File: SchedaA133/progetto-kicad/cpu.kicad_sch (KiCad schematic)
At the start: 77 parts, among them J301 UART0 debug, SW301 RESET, SW302 FEL, U301 A133, U302 TPD4E05U06DQA, U303 TPD4E05U06DQA, U304 TPD4E05U06DQA, U305 TPD4E05U06DQA, U306 TPD4E05U06DQA, U307 TPD4E05U06DQA, Y301 24MHz, Y302 32.768kHz

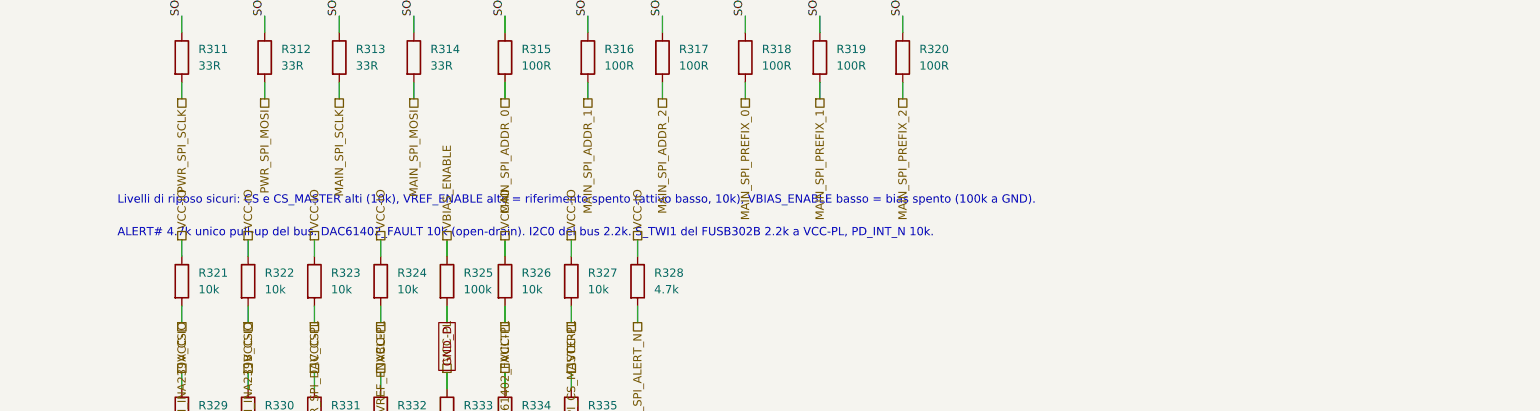
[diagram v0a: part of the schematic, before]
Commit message: SchedaA133: VREF_ENABLE attivo alto e FPC XUNPU
R324 da pull-up a pull-down 10k (VREF_ENABLE ora attivo alto sul modulo
Power). J2 MAIN con footprint XUNPU FPC-05F-28PH20 (LCSC C2856807) al
posto dell'Hirose provvisorio. Schema PDF rigenerato, ERC 0.

Co-Authored-By: Claude Opus 5.5 (1M context) <noreply@anthropic.com>
Claude-Session: https://claude.ai/code/session_01J3krgWFTUEjwvCnwUp9cQn
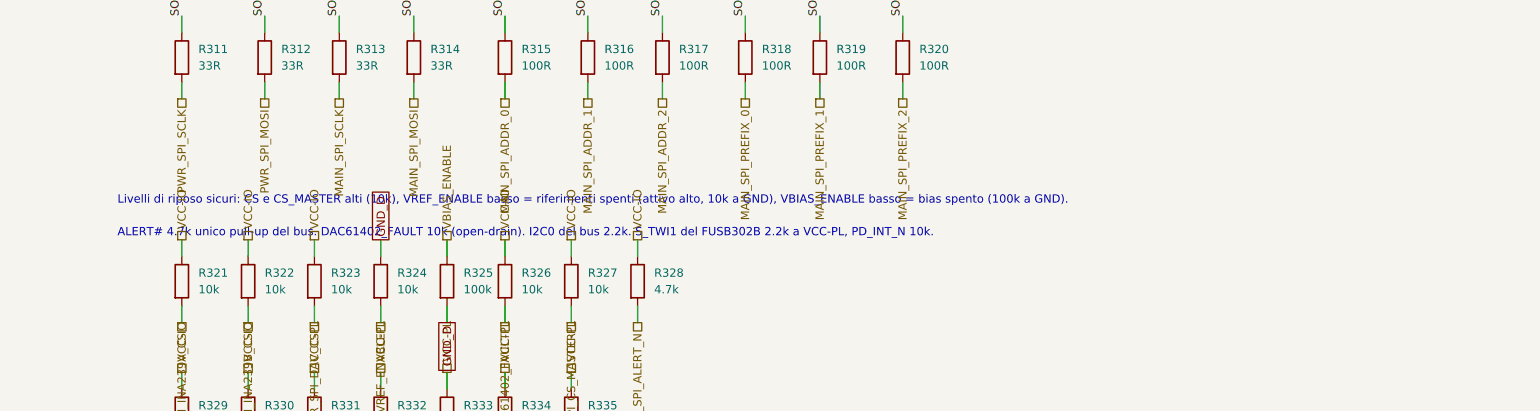
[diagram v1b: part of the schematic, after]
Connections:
- net GND_D: now also R324.1
- net VCC-IO: no longer R324.1
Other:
- note added: "Livelli di riposo sicuri: CS e CS_MASTER alti (10k), VREF_ENABLE basso = riferimenti spenti (attivo alto, 10k a GND), VBIAS_ENABLE basso = bias spento (100k a GND)."
- note removed: "Livelli di riposo sicuri: CS e CS_MASTER alti (10k), VREF_ENABLE alto = riferimento spento (attivo basso, 10k), VBIAS_ENABLE basso = bias spento (100k a GND)."

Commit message: Bus MIKILAB REV5.1: linea di coincidenza HIT# sul pin 28 del MAIN
Specifica: pin 28 (prima GND ridondante) = HIT#, open-drain attivo basso,
pull-up unico 4.7k sul master, impulso 100-200 ns per evento; logica di
coincidenza documentata (fronte marcato dal master, lettura dei latch).
PianoTest: HIT -> monostabile 74LVC1G123 (2k + 27 pF) -> 74LVC1G06 su
HIT#, passante J_IN -> J_OUT, ESD. ERC 0.
SchedaA133: J2 pin 28 -> PD4 (PD_EINT4), pull-up R336 4.7k, ESD su U307,
R337 0R DNP verso l'EXTINT del NEO-F10T. ERC 0, PDF rigenerato.
Documentazione bus della A133 e articolo (sezione bus e coincidenze)
aggiornati; corretta l'identita del primo piano (0).

Co-Authored-By: Claude Opus 5.5 (1M context) <noreply@anthropic.com>
Claude-Session: https://claude.ai/code/session_01J3krgWFTUEjwvCnwUp9cQn
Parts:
- added R336: 4.7k, Resistor_SMD:R_0402_1005Metric, symbol Device:R
- added R337: 0R, Resistor_SMD:R_0402_1005Metric, symbol Device:R
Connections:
- net VCC-IO: now also R336.1
- net MAIN_HIT_N: now reaches U307.4 (D2+)
- net MAIN_HIT_N: now also U301.AA22 (PD4), R336.2, R337.1
- new net GNSS_STROBE_R: R337.2
- no-connect marks 104 -> 102
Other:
- note added: "HIT# (MAIN pin 28, REV5.1): open-drain attivo basso, pull-up unico 4.7k (R336), su PD4 (PD_EINT4). R337 DNP: HIT# anche sull'ingresso time mark del NEO-F10T (EXTINT, fronte di discesa); montarlo solo senza STROBE esterno."

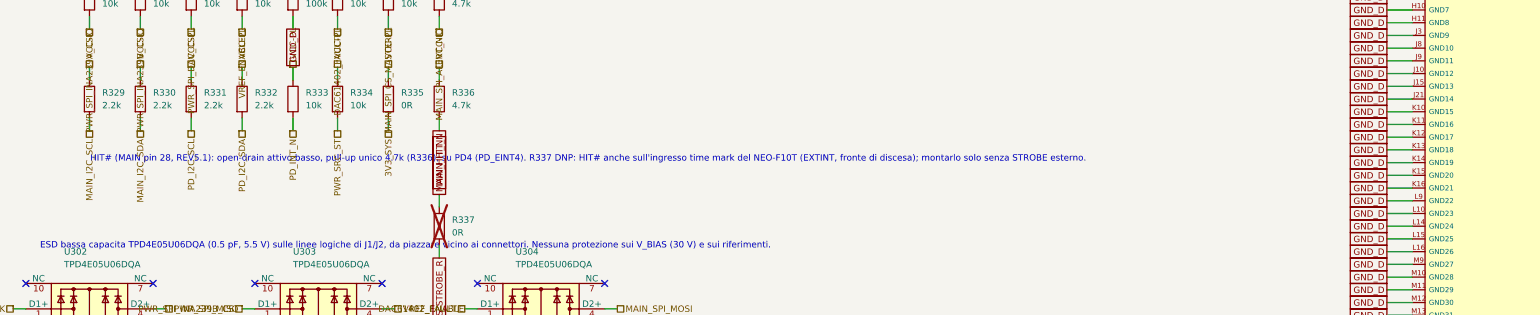
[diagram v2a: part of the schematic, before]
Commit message: SchedaA133: NEO-F10T sostituito dal NEO-M9N-00B
- Simbolo RF_GPS:NEO-M9N, pin verificati sul data sheet UBX-19014285 R08 (tabella 9)
- Collegamenti invariati sui pin comuni; V_USB (pin 7) ora a GND, D_SEL, USB, LNA_EN, SDA/SCL liberi
- README, bom-a133.csv (U10) e documenti aggiornati, eMMC resta 256 GB
- ERC 0, schema-a133.pdf riesportato

Co-Authored-By: Claude Opus 5.5 (1M context) <noreply@anthropic.com>
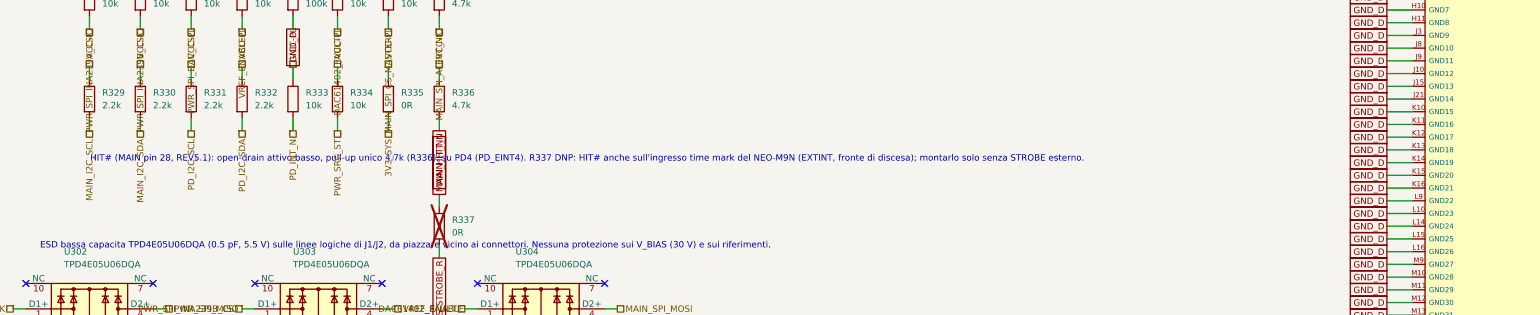
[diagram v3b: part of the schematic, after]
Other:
- note added: "HIT# (MAIN pin 28, REV5.1): open-drain attivo basso, pull-up unico 4.7k (R336), su PD4 (PD_EINT4). R337 DNP: HIT# anche sull'ingresso time mark del NEO-M9N (EXTINT, fronte di discesa); montarlo solo senza STROBE esterno."
- note removed: "HIT# (MAIN pin 28, REV5.1): open-drain attivo basso, pull-up unico 4.7k (R336), su PD4 (PD_EINT4). R337 DNP: HIT# anche sull'ingresso time mark del NEO-F10T (EXTINT, fronte di discesa); montarlo solo senza STROBE esterno."
